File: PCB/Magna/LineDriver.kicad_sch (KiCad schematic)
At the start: 36 parts, among them J1301 Conn_Coaxial, J1302 Conn_Coaxial, U1301 NE5532, U1302 NE5532, U1303 NE5532

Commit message: Add final touched to all schematics
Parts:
- added C1313, C1314, C1315: 100nF/16V, Capacitor_SMD:C_0402_1005Metric, symbol Device:C
- renumbered C1311 to C1301, C1312 to C1302, C1301 to C1303, C1308 to C1304, C1302 to C1305, C1309 to C1306, C1303 to C1307, C1310 to C1308, C1304 to C1309, C1306 to C1310, C1305 to C1311, C1307 to C1312, R1314 to R1302, R1302 to R1303, R1315 to R1304, R1303 to R1305, R1316 to R1306, R1304 to R1307, R1317 to R1308, R1305 to R1309, R1318 to R1310, R1306 to R1311, R1310 to R1312, R1307 to R1313, R1311 to R1314, R1308 to R1315, R1312 to R1316, R1309 to R1317, R1313 to R1318, U1303 to U1302, U1302 to U1303
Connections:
- net GND: now also U1301.4 (V-), U1302.4 (V-), U1303.4 (V-), C1313.2, C1314.2, C1315.2
- net VAA: now reaches U1301.8 (V+)
- net VAA: now also U1302.8 (V+), U1303.8 (V+), C1313.1, C1314.1, C1315.1
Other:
- moved on the sheet: C1301, C1302, C1303, C1304, C1305, C1306, C1307, C1308, C1309, C1310, C1311, C1312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

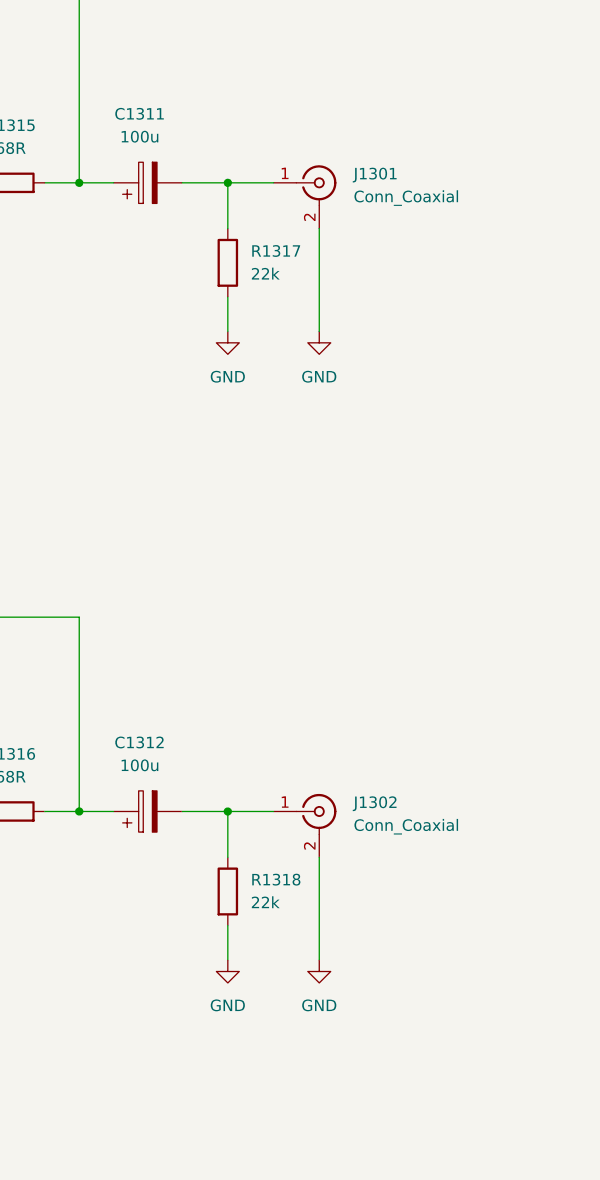
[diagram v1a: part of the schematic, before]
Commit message: Remove all ERC in schematics
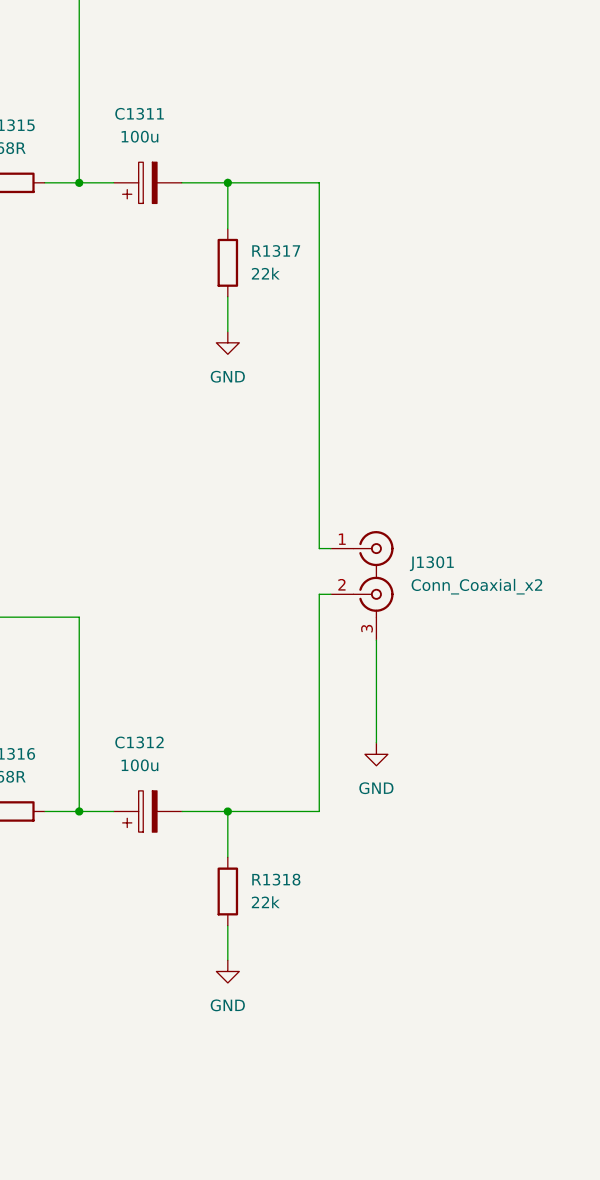
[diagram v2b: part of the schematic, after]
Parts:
- removed J1301, J1302: Conn_Coaxial, symbol Connector:Conn_Coaxial
- added J1301: Conn_Coaxial_x2, symbol Connector:Conn_Coaxial_x2
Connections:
- net GND: now also J1301.3 (EXT)
- net at C1312.2, R1318.1: now also J1301.2 (IN2)
- net at C1311.2, R1317.1: now also J1301.1 (IN1)
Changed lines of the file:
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@@
     (stroke (width 0) (type default))
   )
-  (wire (pts (xy 248.92 115.57) (xy 254 115.57))
+  (wire (pts (xy 248.92 115.57) (xy 259.08 115.57))
     (stroke (width 0) (type default))
   )
@@
     (stroke (width 0) (type default))
   )
+  (wire (pts (xy 260.35 91.44) (xy 259.08 91.44))
+    (stroke (width 0) (type default))
+  )
   (wire (pts (xy 121.92 53.34) (xy 121.92 66.04))
     (stroke (width 0) (type default))
@@
     (stroke (width 0) (type default))
   )
-  (wire (pts (xy 259.08 50.8) (xy 259.08 62.23))
-    (stroke (width 0) (type default))
-  )
   (wire (pts (xy 91.44 165.1) (xy 91.44 167.64))
     (stroke (width 0) (type default))
@@
     (stroke (width 0) (type default))
   )
-  (wire (pts (xy 259.08 120.65) (xy 259.08 132.08))
+  (wire (pts (xy 265.43 96.52) (xy 265.43 107.95))
     (stroke (width 0) (type default))
   )
@@
     (stroke (width 0) (type default))
   )
+  (wire (pts (xy 259.08 91.44) (xy 259.08 115.57))
+    (stroke (width 0) (type default))
+  )
   (wire (pts (xy 243.84 115.57) (xy 248.92 115.57))
     (stroke (width 0) (type default))
@@
     (stroke (width 0) (type default))
   )
+  (wire (pts (xy 259.08 86.36) (xy 259.08 45.72))
+    (stroke (width 0) (type default))
+  )
   (wire (pts (xy 210.82 45.72) (xy 208.28 45.72))
     (stroke (width 0) (type default))
@@
     (stroke (width 0) (type default))
   )
+  (wire (pts (xy 259.08 86.36) (xy 260.35 86.36))
+    (stroke (width 0) (type default))
+  )
   (wire (pts (xy 210.82 105.41) (xy 210.82 115.57))
     (stroke (width 0) (type default))
@@
     (stroke (width 0) (type default))
   )
-  (wire (pts (xy 248.92 45.72) (xy 254 45.72))
+  (wire (pts (xy 248.92 45.72) (xy 259.08 45.72))
     (stroke (width 0) (type default))
   )
@@
     )
   )
+  (symbol (lib_id "Connector:Conn_Coaxial_x2") (at 265.43 88.9 0) (unit 1)
+    (in_bom yes) (on_board yes) (dnp no) (fields_autoplaced)
+    (property "Reference" "J1301" (at 269.24 87.9232 0)
+      (effects (font (size 1.27 1.27)) (justify left))
+    )
+    (property "Value" "Conn_Coaxial_x2" (at 269.24 90.4632 0)
+      (effects (font (size 1.27 1.27)) (justify left))
+    )
+    (property "Footprint" "" (at 265.43 91.44 0)
+      (effects (font (size 1.27 1.27)) hide)
+    )
+    (property "Datasheet" " ~" (at 265.43 91.44 0)
+      (effects (font (size 1.27 1.27)) hide)
+    )
+    (pin "1")
+    (pin "2")
+    (pin "3")
+    (instances
+      (project "Magna"
+        (path "/1469ea1f-a157-49dc-a369-2d42fa17695d/22259812-9e7f-4230-9f2b-a9eb5ce4aaf1/9bed4810-f3e5-480b-be82-dd0796c0885f"
+          (reference "J1301") (unit 1)
+        )
+      )
+    )
+  )
   (symbol (lib_id "Device:C_Polarized") (at 38.1 93.98 90) (unit 1)
     (in_bom yes) (on_board yes) (dnp no) (fields_autoplaced)
@@
     )
   )
-  (symbol (lib_id "Connector:Conn_Coaxial") (at 259.08 115.57 0) (unit 1)
-    (in_bom yes) (on_board yes) (dnp no) (fields_autoplaced)
-    (property "Reference" "J1302" (at 262.89 114.5932 0)
-      (effects (font (size 1.27 1.27)) (justify left))
-    )
-    (property "Value" "Conn_Coaxial" (at 262.89 117.1332 0)
-      (effects (font (size 1.27 1.27)) (justify left))
-    )
-    (property "Footprint" "" (at 259.08 115.57 0)
-      (effects (font (size 1.27 1.27)) hide)
-    )
-    (property "Datasheet" " ~" (at 259.08 115.57 0)
-      (effects (font (size 1.27 1.27)) hide)
-    )
-    (pin "2")
-    (pin "1")
-    (instances
-      (project "Magna"
-        (path "/1469ea1f-a157-49dc-a369-2d42fa17695d/22259812-9e7f-4230-9f2b-a9eb5ce4aaf1/9bed4810-f3e5-480b-be82-dd0796c0885f"
-          (reference "J1302") (unit 1)
-        )
-      )
-    )
-  )
-  (symbol (lib_id "power:GND") (at 259.08 132.08 0) (unit 1)
-    (in_bom yes) (on_board yes) (dnp no) (fields_autoplaced)
-    (property "Reference" "#PWR01306" (at 259.08 138.43 0)
-      (effects (font (size 1.27 1.27)) hide)
-    )
-    (property "Value" "GND" (at 259.08 137.16 0)
-      (effects (font (size 1.27 1.27)))
-    )
-    (property "Footprint" "" (at 259.08 132.08 0)
-      (effects (font (size 1.27 1.27)) hide)
-    )
-    (property "Datasheet" "" (at 259.08 132.08 0)
+  (symbol (lib_id "power:GND") (at 265.43 107.95 0) (unit 1)
+    (in_bom yes) (on_board yes) (dnp no) (fields_autoplaced)
+    (property "Reference" "#PWR01306" (at 265.43 114.3 0)
+      (effects (font (size 1.27 1.27)) hide)
+    )
+    (property "Value" "GND" (at 265.43 113.03 0)
+      (effects (font (size 1.27 1.27)))
+    )
+    (property "Footprint" "" (at 265.43 107.95 0)
+      (effects (font (size 1.27 1.27)) hide)
+    )
+    (property "Datasheet" "" (at 265.43 107.95 0)
       (effects (font (size 1.27 1.27)) hide)
     )
@@
     )
   )
-  (symbol (lib_id "power:GND") (at 259.08 62.23 0) (unit 1)
-    (in_bom yes) (on_board yes) (dnp no) (fields_autoplaced)
-    (property "Reference" "#PWR01305" (at 259.08 68.58 0)
-      (effects (font (size 1.27 1.27)) hide)
-    )
-    (property "Value" "GND" (at 259.08 67.31 0)
-      (effects (font (size 1.27 1.27)))
-    )
-    (property "Footprint" "" (at 259.08 62.23 0)
-      (effects (font (size 1.27 1.27)) hide)
-    )
-    (property "Datasheet" "" (at 259.08 62.23 0)
-      (effects (font (size 1.27 1.27)) hide)
-    )
-    (pin "1")
-    (instances
-      (project "Magna"
-        (path "/1469ea1f-a157-49dc-a369-2d42fa17695d/22259812-9e7f-4230-9f2b-a9eb5ce4aaf1/9bed4810-f3e5-480b-be82-dd0796c0885f"
-          (reference "#PWR01305") (unit 1)
-        )
-      )
-    )
-  )
   (symbol (lib_id "Device:C") (at 200.66 105.41 90) (unit 1)
     (in_bom yes) (on_board yes) (dnp no) (fields_autoplaced)
@@
         )
       )
-    )
-  )
-  (symbol (lib_id "Connector:Conn_Coaxial") (at 259.08 45.72 0) (unit 1)
-    (in_bom yes) (on_board yes) (dnp no) (fields_autoplaced)
-    (property "Reference" "J1301" (at 262.89 44.7432 0)
-      (effects (font (size 1.27 1.27)) (justify left))
-    )
-    (property "Value" "Conn_Coaxial" (at 262.89 47.2832 0)
-      (effects (font (size 1.27 1.27)) (justify left))
-    )
-    (property "Footprint" "" (at 259.08 45.72 0)
-      (effects (font (size 1.27 1.27)) hide)
-    )
-    (property "Datasheet" " ~" (at 259.08 45.72 0)
-      (effects (font (size 1.27 1.27)) hide)
-    )
-    (pin "2")
-    (pin "1")
-    (instances
-      (project "Magna"
-        (path "/1469ea1f-a157-49dc-a369-2d42fa17695d/22259812-9e7f-4230-9f2b-a9eb5ce4aaf1/9bed4810-f3e5-480b-be82-dd0796c0885f"
-          (reference "J1301") (unit 1)
-        )
-      )

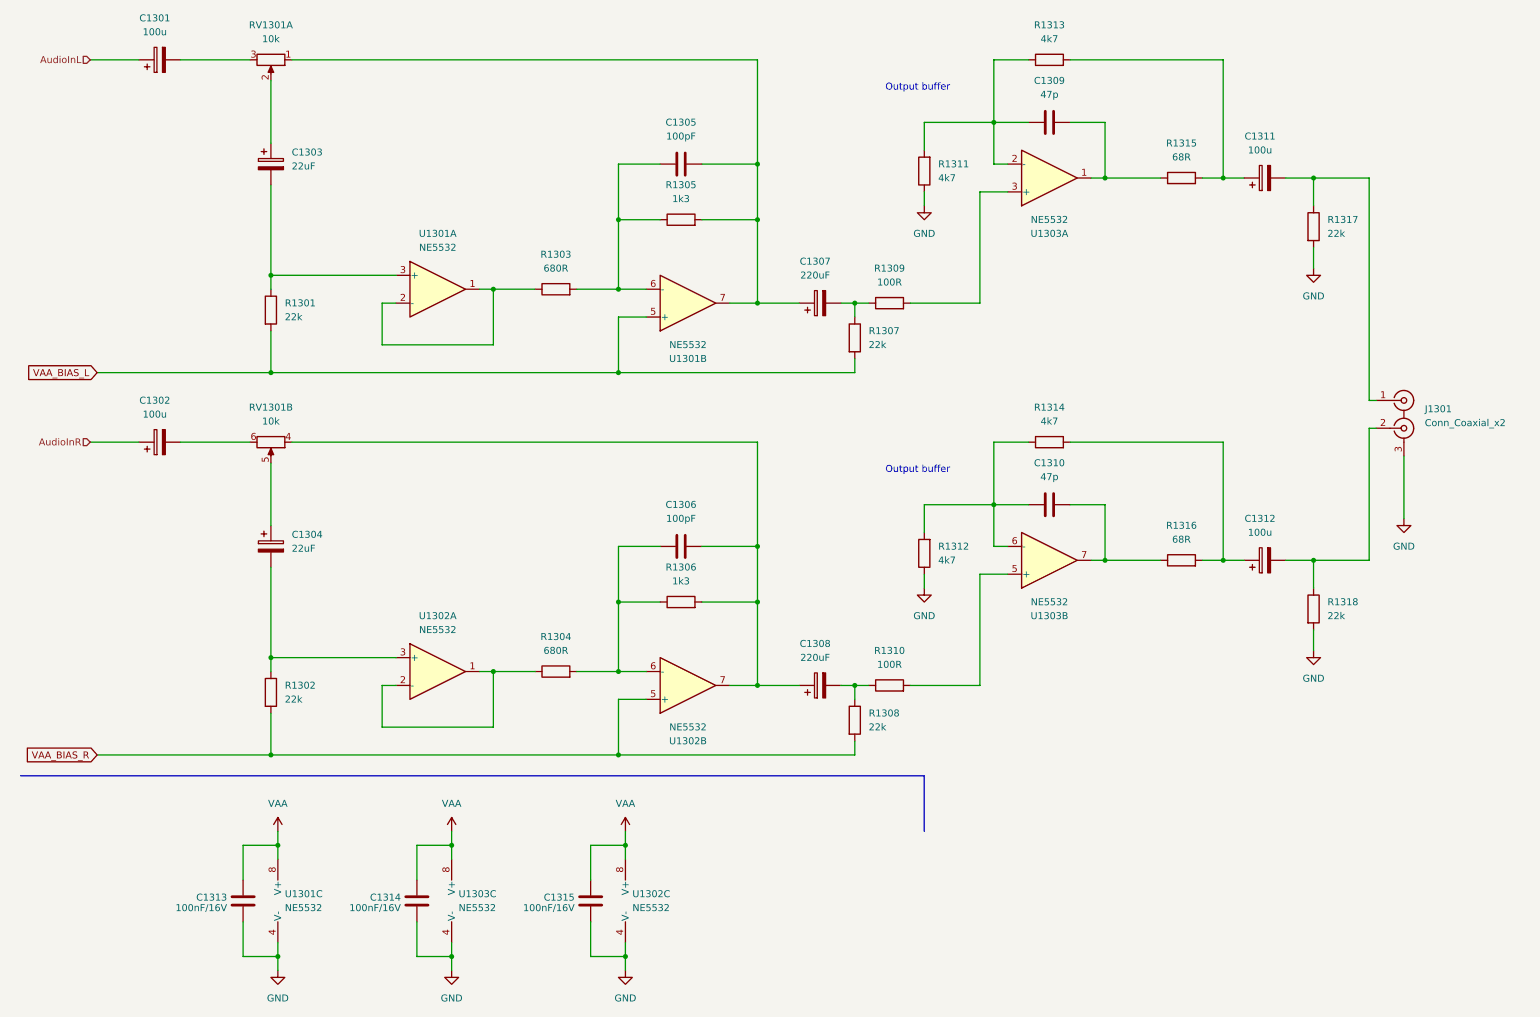
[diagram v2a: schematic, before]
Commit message: Update capacitors to parts in JLC library
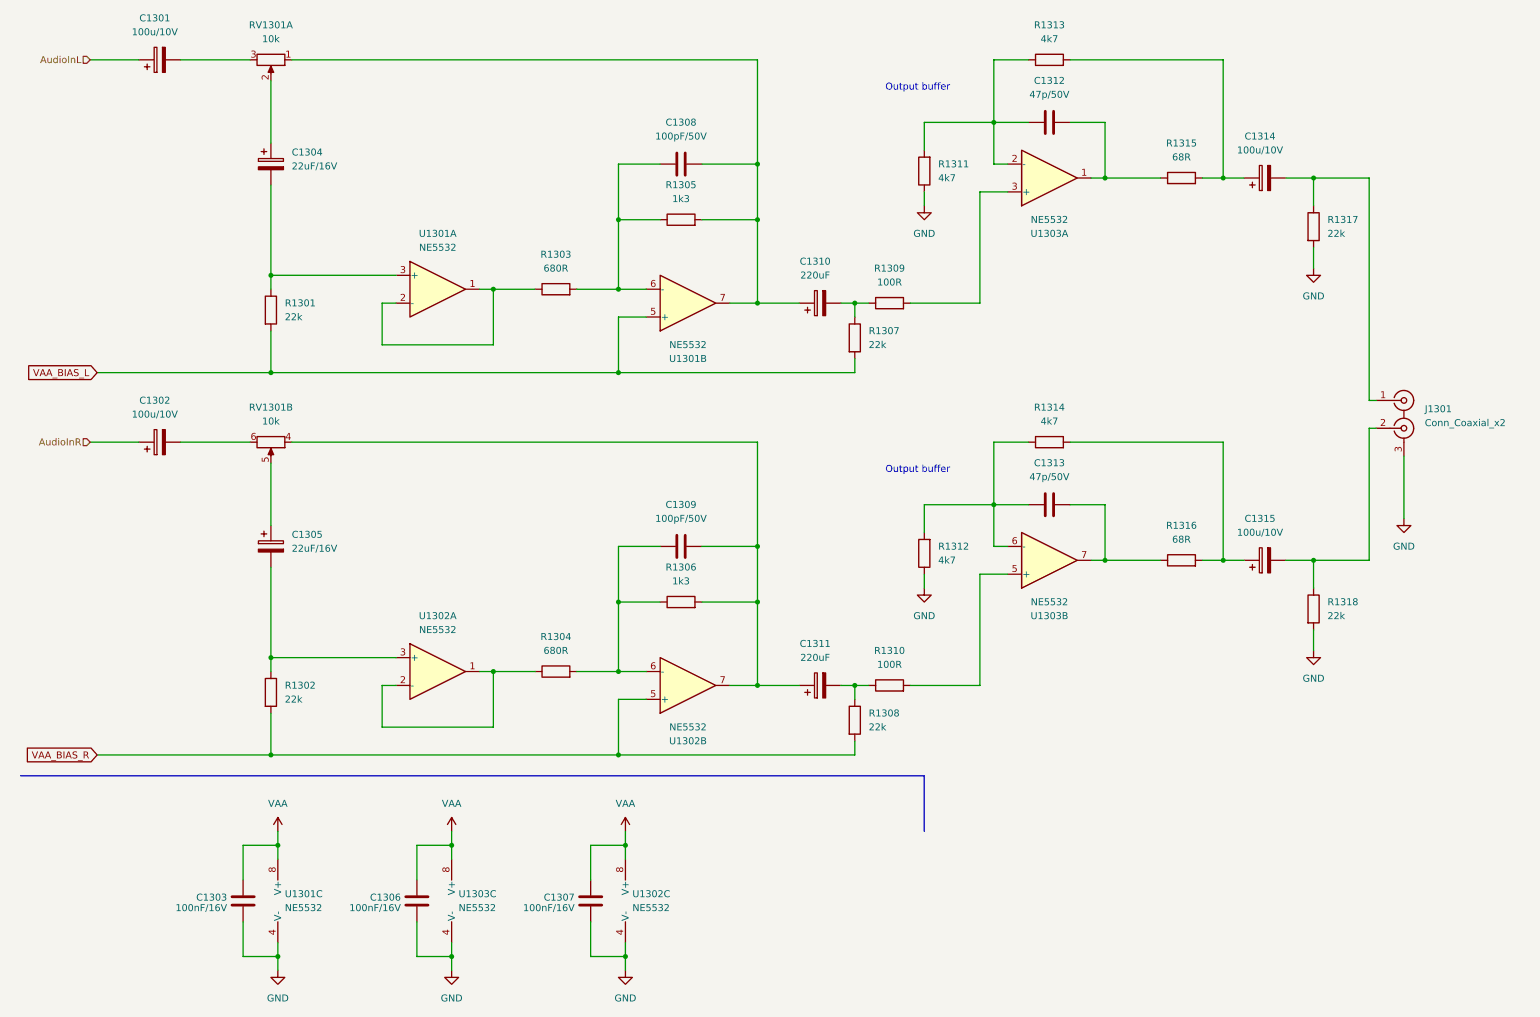
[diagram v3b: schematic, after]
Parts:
- C1301, C1302: value 100u -> 100u/10V; footprint (none) -> Capacitor_SMD:CP_Elec_6.3x5.8; LCSC (none) -> C2166157
- C1303: renamed from C1313; footprint Capacitor_SMD:C_0402_1005Metric -> Capacitor_SMD:C_0805_2012Metric; LCSC C1525 -> C218638
- C1304: renamed from C1303; value 22uF -> 22uF/16V; footprint (none) -> Capacitor_SMD:CP_Elec_5x5.8; LCSC (none) -> C2163245
- C1305: renamed from C1304; value 22uF -> 22uF/16V; footprint (none) -> Capacitor_SMD:CP_Elec_5x5.8; LCSC (none) -> C2163245
- C1306: renamed from C1314; footprint Capacitor_SMD:C_0402_1005Metric -> Capacitor_SMD:C_0805_2012Metric; LCSC C1525 -> C218638
- C1307: renamed from C1315; footprint Capacitor_SMD:C_0402_1005Metric -> Capacitor_SMD:C_0805_2012Metric; LCSC C1525 -> C218638
- C1308: renamed from C1305; value 100pF -> 100pF/50V; footprint (none) -> Capacitor_SMD:C_0805_2012Metric; LCSC (none) -> C1790
- C1309: renamed from C1306; value 100pF -> 100pF/50V; footprint (none) -> Capacitor_SMD:C_0805_2012Metric; LCSC (none) -> C1790
- C1310: renamed from C1307; footprint (none) -> Capacitor_SMD:CP_Elec_4x5.8; LCSC (none) -> C2165067
- C1311: renamed from C1308; footprint (none) -> Capacitor_SMD:CP_Elec_4x5.8; LCSC (none) -> C2165067
- C1312: renamed from C1309; value 47p -> 47p/50V; footprint (none) -> Capacitor_SMD:C_0805_2012Metric; LCSC (none) -> C14857
- C1313: renamed from C1310; value 47p -> 47p/50V; footprint (none) -> Capacitor_SMD:C_0805_2012Metric; LCSC (none) -> C14857
- C1314: renamed from C1311; value 100u -> 100u/10V; footprint (none) -> Capacitor_SMD:CP_Elec_6.3x5.8; LCSC (none) -> C2166157
- C1315: renamed from C1312; value 100u -> 100u/10V; footprint (none) -> Capacitor_SMD:CP_Elec_6.3x5.8; LCSC (none) -> C2166157

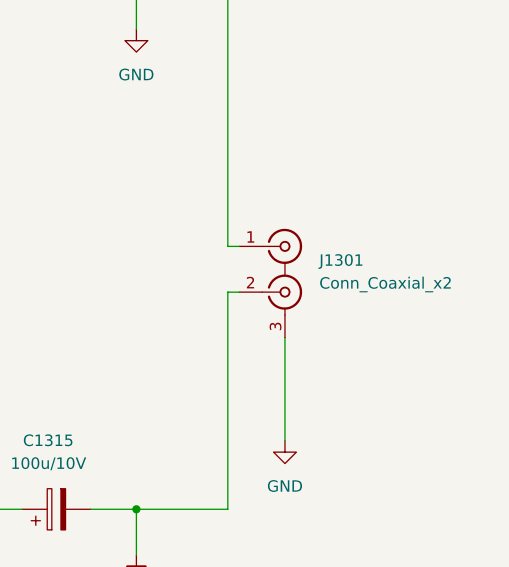
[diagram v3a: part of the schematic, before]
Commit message: Select parts for all components
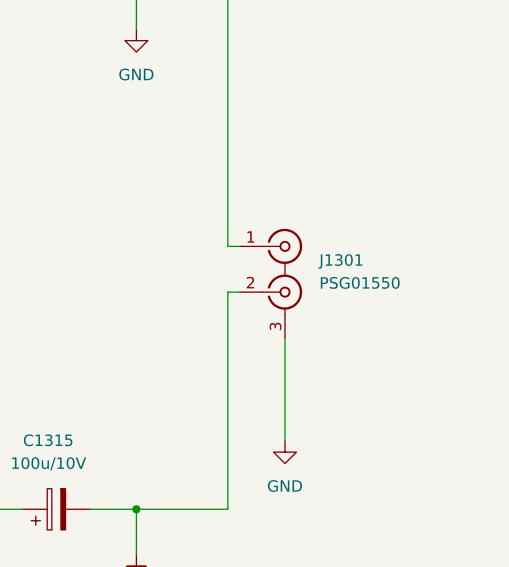
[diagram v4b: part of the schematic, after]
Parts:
- J1301: value Conn_Coaxial_x2 -> PSG01550
- R1301, R1302, R1307, R1308, R1317, R1318: footprint (none) -> Resistor_SMD:R_0805_2012Metric; LCSC (none) -> C479095
- R1303, R1304: footprint (none) -> Resistor_SMD:R_0805_2012Metric_Pad1.20x1.40mm_HandSolder; LCSC (none) -> C865612
- R1305, R1306: footprint (none) -> Resistor_SMD:R_0805_2012Metric_Pad1.20x1.40mm_HandSolder; LCSC (none) -> C218394
- R1309, R1310: footprint (none) -> Resistor_SMD:R_0805_2012Metric_Pad1.20x1.40mm_HandSolder; LCSC (none) -> C217766
- R1311, R1312, R1313, R1314: footprint (none) -> Resistor_SMD:R_0805_2012Metric_Pad1.20x1.40mm_HandSolder; LCSC (none) -> C17673
- R1315, R1316: footprint (none) -> Resistor_SMD:R_0805_2012Metric_Pad1.20x1.40mm_HandSolder; LCSC (none) -> C865616
- U1301, U1302, U1303: LCSC (none) -> C7426
